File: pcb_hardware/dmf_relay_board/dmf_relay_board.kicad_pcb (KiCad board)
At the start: 2 copper layers, 100 x 100 mm, 9 parts, among them J1 HVPS, J2 Relays to Electrodes 1, J3 Relays to Electrodes 2, J4 Electrodes from Relay 1, J5 Electrodes from Relay 2, U1 HV507

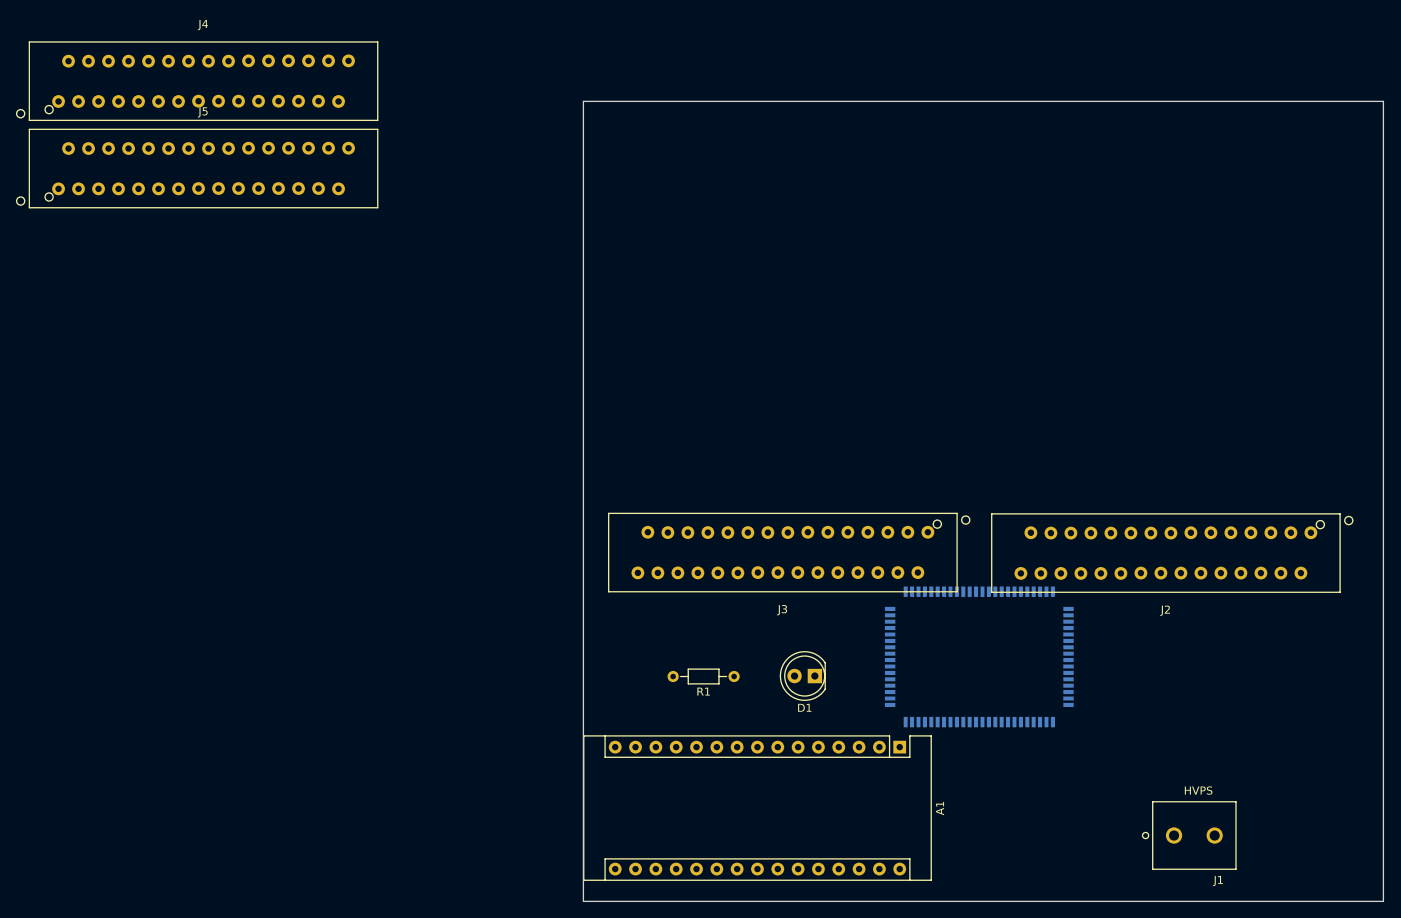
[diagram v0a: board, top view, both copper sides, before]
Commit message: J2 routes complete
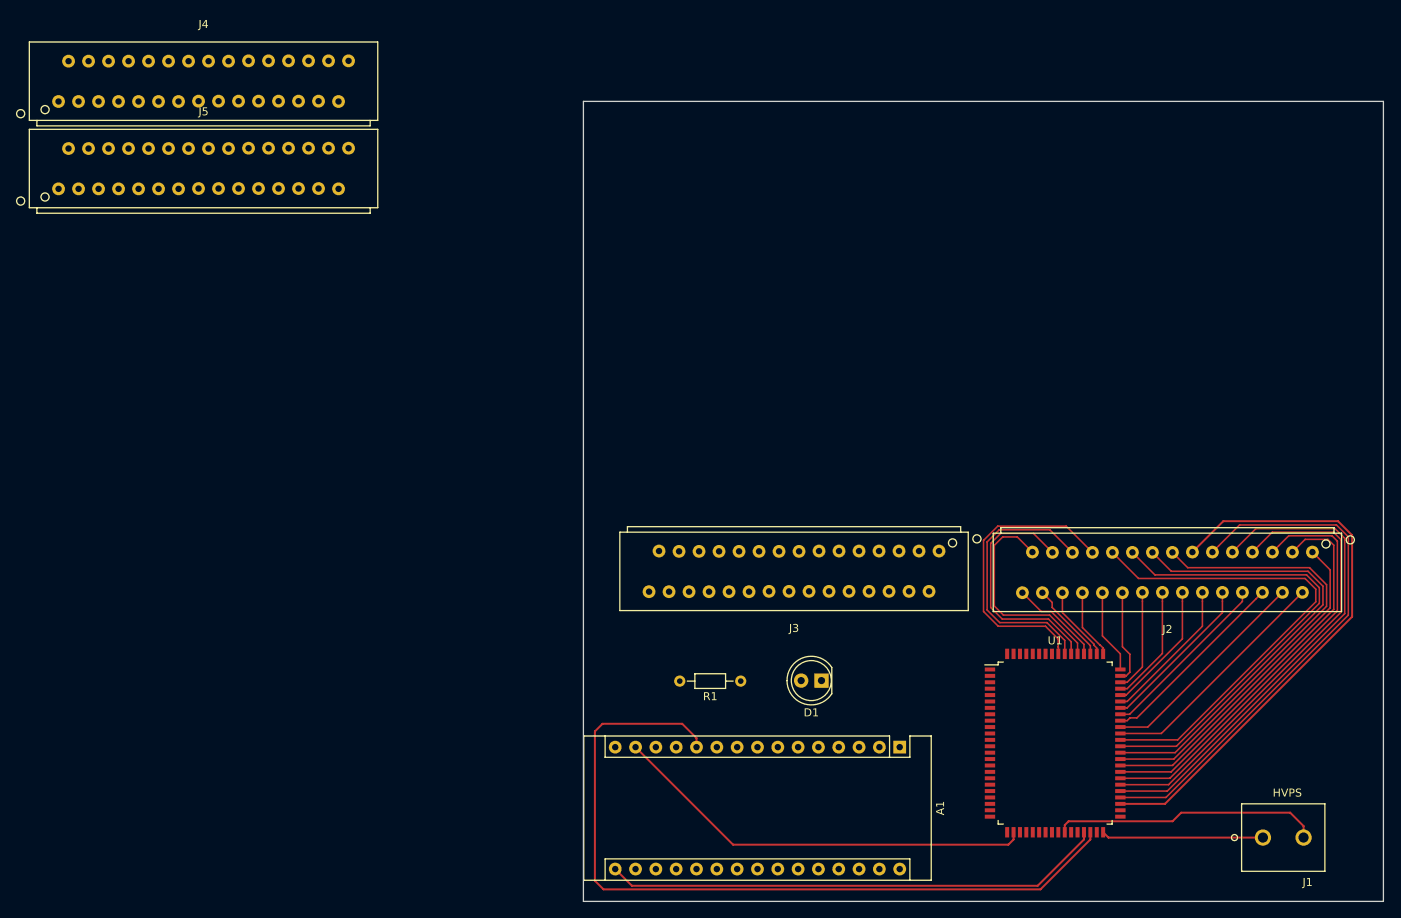
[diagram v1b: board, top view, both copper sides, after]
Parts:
- U1: moved to F.Cu
- moved U1 14.4 mm to (170.9, 130.7), turned to 0 degrees
- moved J1 11.1 mm to (196.9, 142.6)
- moved J3 2.73 mm to (138.3, 109.3)
- moved J2 2.42 mm to (185.0, 109.4)
- moved D1 1.00 mm to (141.7, 122.9)
- moved R1 1.00 mm to (131.6, 123.0)
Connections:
- net ELEC_26 renamed CHNL_26
- net ELEC_29 renamed CHNL_29
- J2 pad 1: ELEC_1 -> CHNL_9
- J2 pad 10: ELEC_10 -> CHNL_18
- J2 pad 11: ELEC_11 -> CHNL_4
- J2 pad 12: ELEC_12 -> CHNL_19
- J2 pad 13: ELEC_13 -> CHNL_3
- J2 pad 14: ELEC_14 -> CHNL_20
- J2 pad 15: ELEC_15 -> CHNL_10
- J2 pad 16: ELEC_16 -> CHNL_21
- J2 pad 17: ELEC_17 -> CHNL_11
- J2 pad 18: ELEC_18 -> CHNL_22
- J2 pad 19: ELEC_19 -> CHNL_12
- J2 pad 2: ELEC_2 -> CHNL_14
- J2 pad 20: ELEC_20 -> CHNL_23
- J2 pad 21: ELEC_21 -> CHNL_13
- J2 pad 22: ELEC_22 -> CHNL_24
- J2 pad 23: ELEC_23 -> CHNL_32
- J2 pad 24: ELEC_24 -> CHNL_25
- J2 pad 25: ELEC_25 -> CHNL_31
- J2 pad 27: ELEC_27 -> CHNL_30
- J2 pad 28: ELEC_28 -> CHNL_27
- J2 pad 3: ELEC_3 -> CHNL_8
- J2 pad 30: ELEC_30 -> CHNL_28
- J2 pad 4: ELEC_4 -> CHNL_15
- J2 pad 5: ELEC_5 -> CHNL_7
- J2 pad 6: ELEC_6 -> CHNL_16
- J2 pad 7: ELEC_7 -> CHNL_6
- J2 pad 8: ELEC_8 -> CHNL_17
- J2 pad 9: ELEC_9 -> CHNL_5
- J3 pad 1: ELEC_31 -> Net-(J3-Pad1)
- J3 pad 10: ELEC_40 -> Net-(J3-Pad10)
- J3 pad 11: ELEC_41 -> Net-(J3-Pad11)
- J3 pad 12: ELEC_42 -> Net-(J3-Pad12)
- J3 pad 13: ELEC_43 -> Net-(J3-Pad13)
- J3 pad 14: ELEC_44 -> Net-(J3-Pad14)
- J3 pad 15: ELEC_45 -> Net-(J3-Pad15)
- J3 pad 16: ELEC_46 -> Net-(J3-Pad16)
- J3 pad 17: ELEC_47 -> Net-(J3-Pad17)
- J3 pad 18: ELEC_48 -> Net-(J3-Pad18)
- J3 pad 19: ELEC_49 -> Net-(J3-Pad19)
- J3 pad 2: ELEC_32 -> Net-(J3-Pad2)
- J3 pad 20: ELEC_50 -> Net-(J3-Pad20)
- J3 pad 21: ELEC_51 -> Net-(J3-Pad21)
- J3 pad 22: ELEC_52 -> Net-(J3-Pad22)
- J3 pad 23: ELEC_53 -> Net-(J3-Pad23)
- J3 pad 24: ELEC_54 -> Net-(J3-Pad24)
- J3 pad 25: ELEC_55 -> Net-(J3-Pad25)
- J3 pad 26: ELEC_56 -> Net-(J3-Pad26)
- J3 pad 27: ELEC_57 -> Net-(J3-Pad27)
- J3 pad 28: ELEC_58 -> Net-(J3-Pad28)
- J3 pad 29: ELEC_59 -> Net-(J3-Pad29)
- J3 pad 3: ELEC_33 -> Net-(J3-Pad3)
- J3 pad 30: ELEC_60 -> Net-(J3-Pad30)
- J3 pad 4: ELEC_34 -> Net-(J3-Pad4)
- J3 pad 5: ELEC_35 -> Net-(J3-Pad5)
- J3 pad 6: ELEC_36 -> Net-(J3-Pad6)
- J3 pad 7: ELEC_37 -> Net-(J3-Pad7)
- J3 pad 8: ELEC_38 -> Net-(J3-Pad8)
- J3 pad 9: ELEC_39 -> Net-(J3-Pad9)
- U1 pad 1: ELEC_41 -> Net-(U1-Pad1)
- U1 pad 10: ELEC_50 -> Net-(U1-Pad10)
- U1 pad 11: ELEC_51 -> Net-(U1-Pad11)
- U1 pad 12: ELEC_52 -> Net-(U1-Pad12)
- U1 pad 13: ELEC_53 -> Net-(U1-Pad13)
- U1 pad 14: ELEC_54 -> Net-(U1-Pad14)
- U1 pad 15: ELEC_55 -> Net-(U1-Pad15)
- U1 pad 16: ELEC_56 -> Net-(U1-Pad16)
- U1 pad 17: ELEC_57 -> Net-(U1-Pad17)
- U1 pad 18: ELEC_58 -> Net-(U1-Pad18)
- U1 pad 19: ELEC_59 -> Net-(U1-Pad19)
- U1 pad 2: ELEC_42 -> Net-(U1-Pad2)
- U1 pad 20: ELEC_60 -> Net-(U1-Pad20)
- U1 pad 3: ELEC_43 -> Net-(U1-Pad3)
- U1 pad 4: ELEC_44 -> Net-(U1-Pad4)
- U1 pad 41: ELEC_1 -> Net-(U1-Pad41)
- U1 pad 42: ELEC_2 -> Net-(U1-Pad42)
- U1 pad 43: ELEC_3 -> CHNL_3
- U1 pad 44: ELEC_4 -> CHNL_4
- U1 pad 45: ELEC_5 -> CHNL_5
- U1 pad 46: ELEC_6 -> CHNL_6
- U1 pad 47: ELEC_7 -> CHNL_7
- U1 pad 48: ELEC_8 -> CHNL_8
- U1 pad 49: ELEC_9 -> CHNL_9
- U1 pad 5: ELEC_45 -> Net-(U1-Pad5)
- U1 pad 50: ELEC_10 -> CHNL_10
- U1 pad 51: ELEC_11 -> CHNL_11
- U1 pad 52: ELEC_12 -> CHNL_12
- U1 pad 53: ELEC_13 -> CHNL_13
- U1 pad 54: ELEC_14 -> CHNL_14
- U1 pad 55: ELEC_15 -> CHNL_15
- U1 pad 56: ELEC_16 -> CHNL_16
- U1 pad 57: ELEC_17 -> CHNL_17
- U1 pad 58: ELEC_18 -> CHNL_18
- U1 pad 59: ELEC_19 -> CHNL_19
- U1 pad 6: ELEC_46 -> Net-(U1-Pad6)
- U1 pad 60: ELEC_20 -> CHNL_20
- U1 pad 61: ELEC_21 -> CHNL_21
- U1 pad 62: ELEC_22 -> CHNL_22
- U1 pad 63: ELEC_23 -> CHNL_23
- U1 pad 64: ELEC_24 -> CHNL_24
- U1 pad 65: ELEC_25 -> CHNL_25
- U1 pad 67: ELEC_27 -> CHNL_27
- U1 pad 68: ELEC_28 -> CHNL_28
- U1 pad 7: ELEC_47 -> Net-(U1-Pad7)
- U1 pad 70: ELEC_30 -> CHNL_30
- U1 pad 71: ELEC_31 -> CHNL_31
- U1 pad 72: ELEC_32 -> CHNL_32
- U1 pad 73: ELEC_33 -> Net-(U1-Pad73)
- U1 pad 74: ELEC_34 -> Net-(U1-Pad74)
- U1 pad 75: ELEC_35 -> Net-(U1-Pad75)
- U1 pad 76: ELEC_36 -> Net-(U1-Pad76)
- U1 pad 77: ELEC_37 -> Net-(U1-Pad77)
- U1 pad 78: ELEC_38 -> Net-(U1-Pad78)
- U1 pad 79: ELEC_39 -> Net-(U1-Pad79)
- U1 pad 8: ELEC_48 -> Net-(U1-Pad8)
- U1 pad 80: ELEC_40 -> Net-(U1-Pad80)
- U1 pad 9: ELEC_49 -> Net-(U1-Pad9)
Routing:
- net ~LE: track 0.00 -> 99.5 mm
- net CHNL_3: track 0.00 -> 71.1 mm
- net CHNL_4: track 0.00 -> 66.7 mm
- net SCLK: track 0.00 -> 62.8 mm
- net CHNL_5: track 0.00 -> 62.4 mm
- net CHNL_13: track 0.00 -> 60.5 mm
- net CHNL_12: track 0.00 -> 59.4 mm
- net CHNL_11: track 0.00 -> 58.4 mm
- net CHNL_6: track 0.00 -> 58.1 mm
- net CHNL_10: track 0.00 -> 57.3 mm
- net CHNL_7: track 0.00 -> 53.7 mm
- net DI: track 0.00 -> 53.5 mm
- net CHNL_8: track 0.00 -> 49.2 mm
- net CHNL_9: track 0.00 -> 42.3 mm
- net CHNL_32: track 0.00 -> 37.2 mm
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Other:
- net class DMF_HV added: clearance 0.25, trace_width 0.2, via_dia 0.8, via_drill 0.4

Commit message: HV routing complete
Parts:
- moved D1 9.34 mm to (132.4, 123.3)
- moved R1 6.61 mm to (125.0, 123.4)
- moved U1 1.84 mm to (170.9, 132.6)
- moved A1 0.20 mm to (151.4, 131.1)
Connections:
- net VPP+ renamed VPP
- J1 pad 2: VPP- -> GND
- J3 pad 1: Net-(J3-Pad1) -> CHNL_36
- J3 pad 10: Net-(J3-Pad10) -> CHNL_41
- J3 pad 11: Net-(J3-Pad11) -> CHNL_60
- J3 pad 12: Net-(J3-Pad12) -> CHNL_42
- J3 pad 13: Net-(J3-Pad13) -> CHNL_61
- J3 pad 14: Net-(J3-Pad14) -> CHNL_43
- J3 pad 15: Net-(J3-Pad15) -> CHNL_62
- J3 pad 16: Net-(J3-Pad16) -> CHNL_44
- J3 pad 17: Net-(J3-Pad17) -> CHNL_58
- J3 pad 18: Net-(J3-Pad18) -> CHNL_45
- J3 pad 19: Net-(J3-Pad19) -> CHNL_57
- J3 pad 2: Net-(J3-Pad2) -> CHNL_37
- J3 pad 20: Net-(J3-Pad20) -> CHNL_46
- J3 pad 21: Net-(J3-Pad21) -> CHNL_56
- J3 pad 22: Net-(J3-Pad22) -> CHNL_47
- J3 pad 23: Net-(J3-Pad23) -> CHNL_55
- J3 pad 24: Net-(J3-Pad24) -> CHNL_48
- J3 pad 25: Net-(J3-Pad25) -> CHNL_54
- J3 pad 26: Net-(J3-Pad26) -> CHNL_49
- J3 pad 27: Net-(J3-Pad27) -> CHNL_53
- J3 pad 28: Net-(J3-Pad28) -> CHNL_50
- J3 pad 29: Net-(J3-Pad29) -> CHNL_52
- J3 pad 3: Net-(J3-Pad3) -> CHNL_35
- J3 pad 30: Net-(J3-Pad30) -> CHNL_51
- J3 pad 4: Net-(J3-Pad4) -> CHNL_38
- J3 pad 5: Net-(J3-Pad5) -> CHNL_34
- J3 pad 6: Net-(J3-Pad6) -> CHNL_39
- J3 pad 7: Net-(J3-Pad7) -> CHNL_33
- J3 pad 8: Net-(J3-Pad8) -> CHNL_40
- J3 pad 9: Net-(J3-Pad9) -> CHNL_59
- U1 pad 1: Net-(U1-Pad1) -> CHNL_41
- U1 pad 10: Net-(U1-Pad10) -> CHNL_50
- U1 pad 11: Net-(U1-Pad11) -> CHNL_51
- U1 pad 12: Net-(U1-Pad12) -> CHNL_52
- U1 pad 13: Net-(U1-Pad13) -> CHNL_53
- U1 pad 14: Net-(U1-Pad14) -> CHNL_54
- U1 pad 15: Net-(U1-Pad15) -> CHNL_55
- U1 pad 16: Net-(U1-Pad16) -> CHNL_56
- U1 pad 17: Net-(U1-Pad17) -> CHNL_57
- U1 pad 18: Net-(U1-Pad18) -> CHNL_58
- U1 pad 19: Net-(U1-Pad19) -> CHNL_59
- U1 pad 2: Net-(U1-Pad2) -> CHNL_42
- U1 pad 20: Net-(U1-Pad20) -> CHNL_60
- U1 pad 21: Net-(U1-Pad21) -> CHNL_61
- U1 pad 22: Net-(U1-Pad22) -> CHNL_62
- U1 pad 3: Net-(U1-Pad3) -> CHNL_43
- U1 pad 34: VPP- -> GND
- U1 pad 4: Net-(U1-Pad4) -> CHNL_44
- U1 pad 5: Net-(U1-Pad5) -> CHNL_45
- U1 pad 6: Net-(U1-Pad6) -> CHNL_46
- U1 pad 7: Net-(U1-Pad7) -> CHNL_47
- U1 pad 73: Net-(U1-Pad73) -> CHNL_33
- U1 pad 74: Net-(U1-Pad74) -> CHNL_34
- U1 pad 75: Net-(U1-Pad75) -> CHNL_35
- U1 pad 76: Net-(U1-Pad76) -> CHNL_36
- U1 pad 77: Net-(U1-Pad77) -> CHNL_37
- U1 pad 78: Net-(U1-Pad78) -> CHNL_38
- U1 pad 79: Net-(U1-Pad79) -> CHNL_39
- U1 pad 8: Net-(U1-Pad8) -> CHNL_48
- U1 pad 80: Net-(U1-Pad80) -> CHNL_40
- U1 pad 9: Net-(U1-Pad9) -> CHNL_49
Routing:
- net CHNL_54: track 0.00 -> 72.7 mm, vias 0 -> 1
- net CHNL_62: track 0.00 -> 68.8 mm, vias 0 -> 1
- net CHNL_53: track 0.00 -> 68.3 mm, vias 0 -> 1
- net CHNL_61: track 0.00 -> 63.0 mm, vias 0 -> 1
- net CHNL_52: track 0.00 -> 60.7 mm, vias 0 -> 1
- net CHNL_55: track 0.00 -> 58.5 mm, vias 0 -> 1
- net CHNL_56: track 0.00 -> 58.2 mm, vias 0 -> 1
- net CHNL_60: track 0.00 -> 58.1 mm, vias 0 -> 1
- net CHNL_57: track 0.00 -> 57.8 mm, vias 0 -> 1
- net CHNL_58: track 0.00 -> 57.3 mm, vias 0 -> 1
- net CHNL_59: track 0.00 -> 53.0 mm, vias 0 -> 1
- net CHNL_51: track 0.00 -> 50.7 mm, vias 0 -> 1
- net GND: track 0.00 -> 50.1 mm, vias 0 -> 1
- net CHNL_50: track 0.00 -> 47.9 mm, vias 0 -> 1
- net ~BL: track 0.00 -> 47.0 mm, vias 0 -> 1
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- added copper zone on F.Cu, net GND
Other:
- net class DMF_HV: via_dia 0.8 -> 0.6; via_drill 0.4 -> 0.3
- net class Default: via_dia 0.8 -> 0.6; via_drill 0.4 -> 0.3
- net class LV_Power added: clearance 0.2, trace_width 0.35, via_dia 0.6, via_drill 0.3

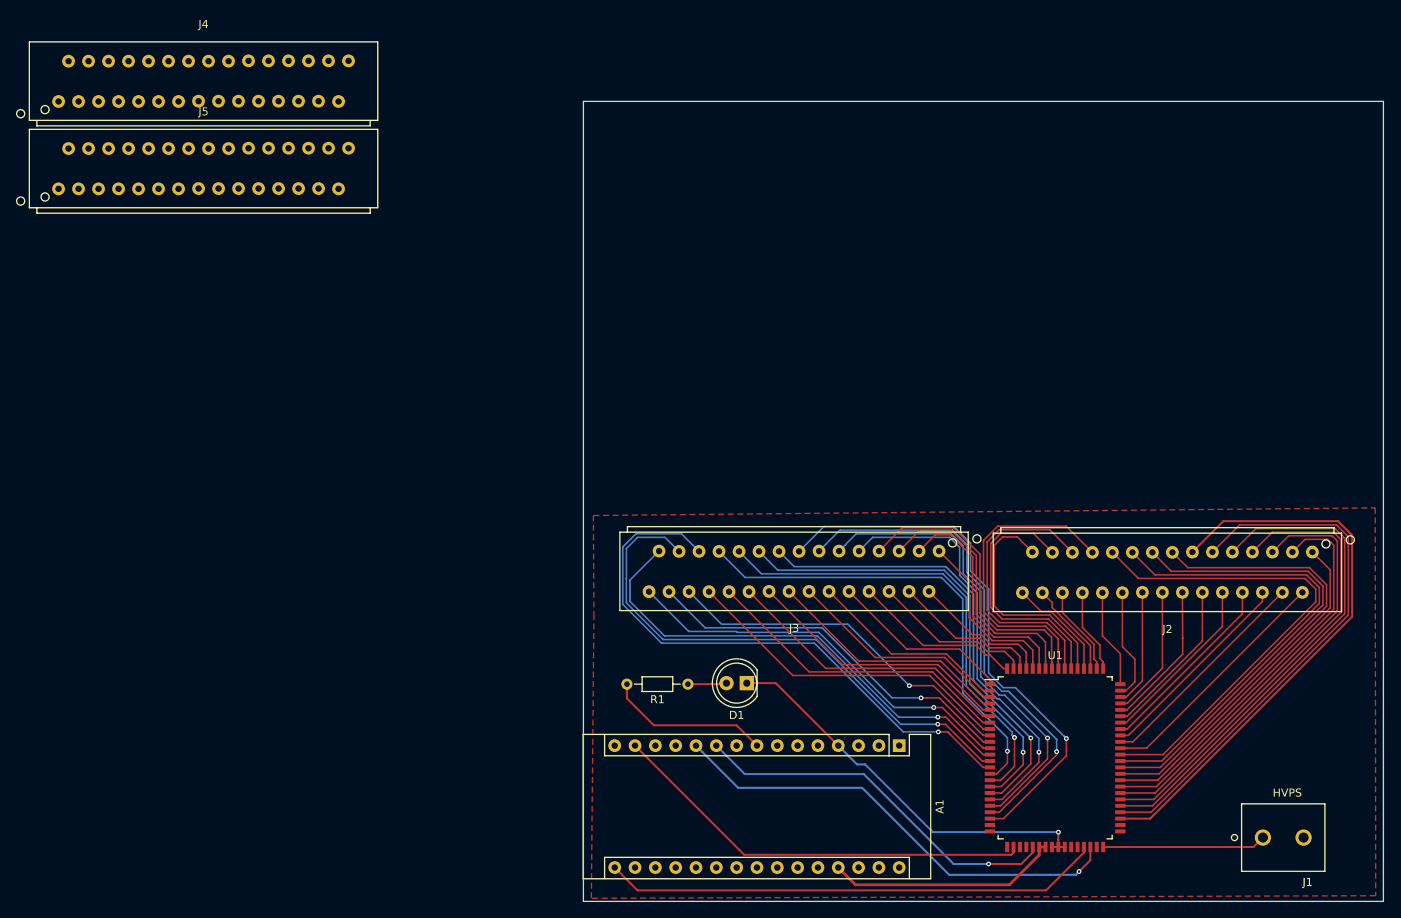
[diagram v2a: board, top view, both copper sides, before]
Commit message: small footprint added
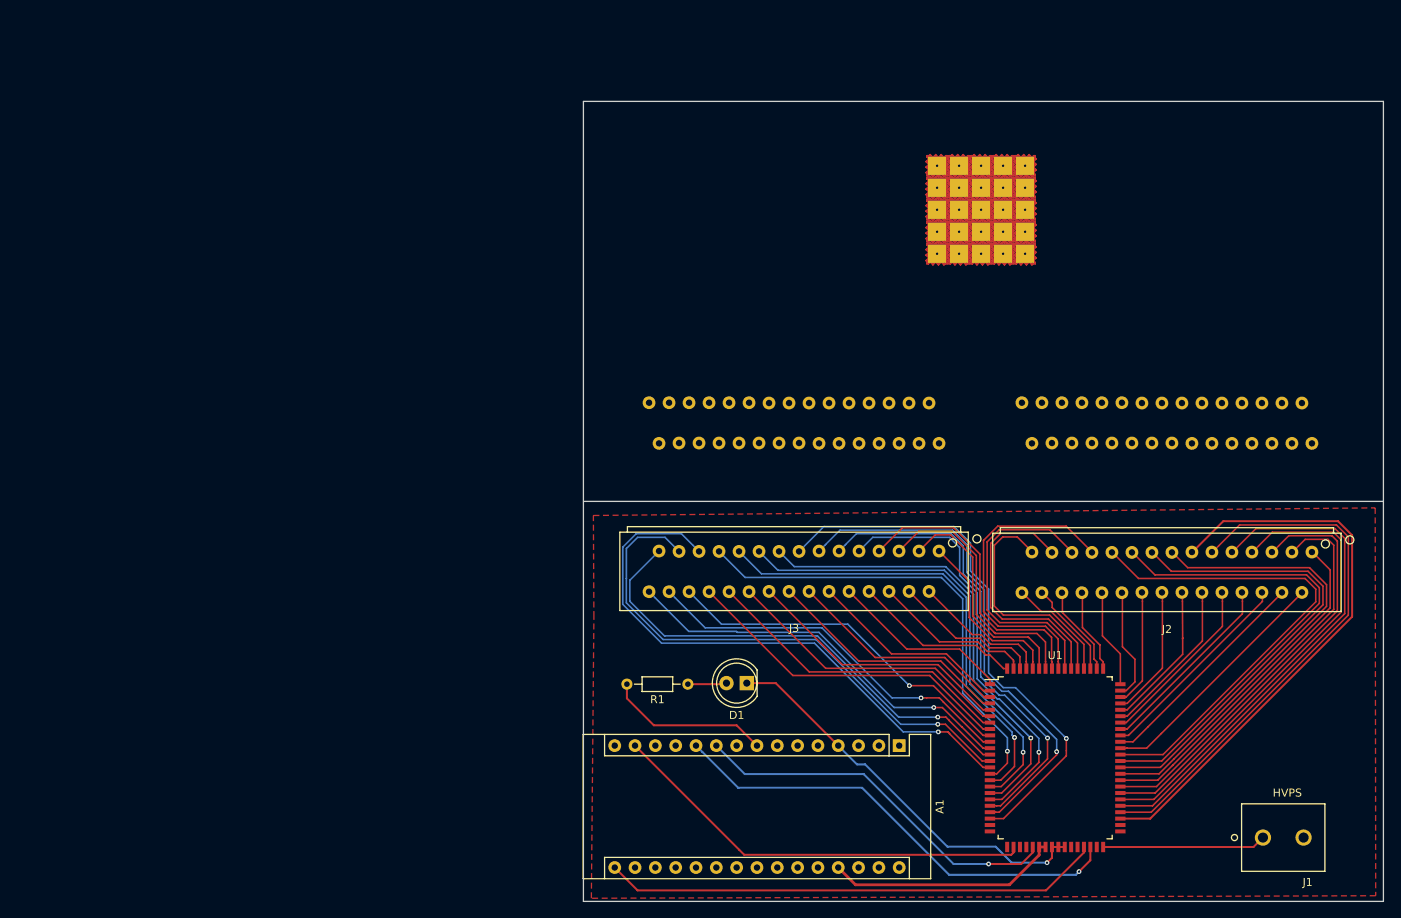
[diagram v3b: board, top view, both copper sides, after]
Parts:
- added ELEC_1: FX, GaudiLabsFootPrints:FLUXPAD_2_75_4MIL_4_5, F.Cu at (167.2, 69.6)
- added ELEC_1: FX, GaudiLabsFootPrints:FLUXPAD_2_75_4MIL_4_5, F.Cu at (156.2, 66.8)
- added ELEC_1: FX, GaudiLabsFootPrints:FLUXPAD_2_75_4MIL_4_5, F.Cu at (167.2, 64.1)
- added ELEC_1: FX, GaudiLabsFootPrints:FLUXPAD_2_75_4MIL_4_5, F.Cu at (164.4, 64.1)
- added ELEC_1: FX, GaudiLabsFootPrints:FLUXPAD_2_75_4MIL_4_5, F.Cu at (161.7, 64.1)
- added ELEC_1: FX, GaudiLabsFootPrints:FLUXPAD_2_75_4MIL_4_5, F.Cu at (158.9, 64.1)
- added ELEC_1: FX, GaudiLabsFootPrints:FLUXPAD_2_75_4MIL_4_5, F.Cu at (156.2, 64.1)
- added ELEC_1: FX, GaudiLabsFootPrints:FLUXPAD_2_75_4MIL_4_5, F.Cu at (167.2, 61.3)
- added ELEC_1: FX, GaudiLabsFootPrints:FLUXPAD_2_75_4MIL_4_5, F.Cu at (164.4, 61.3)
- added ELEC_1: FX, GaudiLabsFootPrints:FLUXPAD_2_75_4MIL_4_5, F.Cu at (161.7, 61.3)
- added ELEC_1: FX, GaudiLabsFootPrints:FLUXPAD_2_75_4MIL_4_5, F.Cu at (158.9, 61.3)
- added ELEC_1: FX, GaudiLabsFootPrints:FLUXPAD_2_75_4MIL_4_5, F.Cu at (164.4, 69.6)
- added ELEC_1: FX, GaudiLabsFootPrints:FLUXPAD_2_75_4MIL_4_5, F.Cu at (156.2, 61.3)
- added ELEC_1: FX, GaudiLabsFootPrints:FLUXPAD_2_75_4MIL_4_5, F.Cu at (167.2, 58.6)
- added ELEC_1: FX, GaudiLabsFootPrints:FLUXPAD_2_75_4MIL_4_5, F.Cu at (164.4, 58.6)
- added ELEC_1: FX, GaudiLabsFootPrints:FLUXPAD_2_75_4MIL_4_5, F.Cu at (161.7, 58.6)
- added ELEC_1: FX, GaudiLabsFootPrints:FLUXPAD_2_75_4MIL_4_5, F.Cu at (158.9, 58.6)
- added ELEC_1: FX, GaudiLabsFootPrints:FLUXPAD_2_75_4MIL_4_5, F.Cu at (156.2, 58.6)
- added ELEC_1: FX, GaudiLabsFootPrints:FLUXPAD_2_75_4MIL_4_5, F.Cu at (161.7, 69.6)
- added ELEC_1: FX, GaudiLabsFootPrints:FLUXPAD_2_75_4MIL_4_5, F.Cu at (158.9, 69.6)
- added ELEC_1: FX, GaudiLabsFootPrints:FLUXPAD_2_75_4MIL_4_5, F.Cu at (156.2, 69.6)
- added ELEC_1: FX, GaudiLabsFootPrints:FLUXPAD_2_75_4MIL_4_5, F.Cu at (167.2, 66.8)
- added ELEC_1: FX, GaudiLabsFootPrints:FLUXPAD_2_75_4MIL_4_5, F.Cu at (164.4, 66.8)
- added ELEC_1: FX, GaudiLabsFootPrints:FLUXPAD_2_75_4MIL_4_5, F.Cu at (161.7, 66.8)
- added ELEC_1: FX, GaudiLabsFootPrints:FLUXPAD_2_75_4MIL_4_5, F.Cu at (158.9, 66.8)
- J4, J5: moved to B.Cu
- moved J4 127.8 mm to (184.9, 90.7), turned to 180 degrees
- moved J5 80.4 mm to (138.3, 90.7), turned to 180 degrees
- moved J2 0.06 mm to (184.9, 109.4)
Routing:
- net GND: track 50.1 -> 50.6 mm
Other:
- outline, holes or cut-outs redrawn
